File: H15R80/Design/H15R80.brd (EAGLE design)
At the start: 34.6 x 30 mm, 49 parts, among them P1 HEXABIT_17.32_NO_P3_P6, U1 STM32F091CBU6, U2 DAC8760RHA, U3 OPA192, X1 XTALL_CSTCE8M00G52

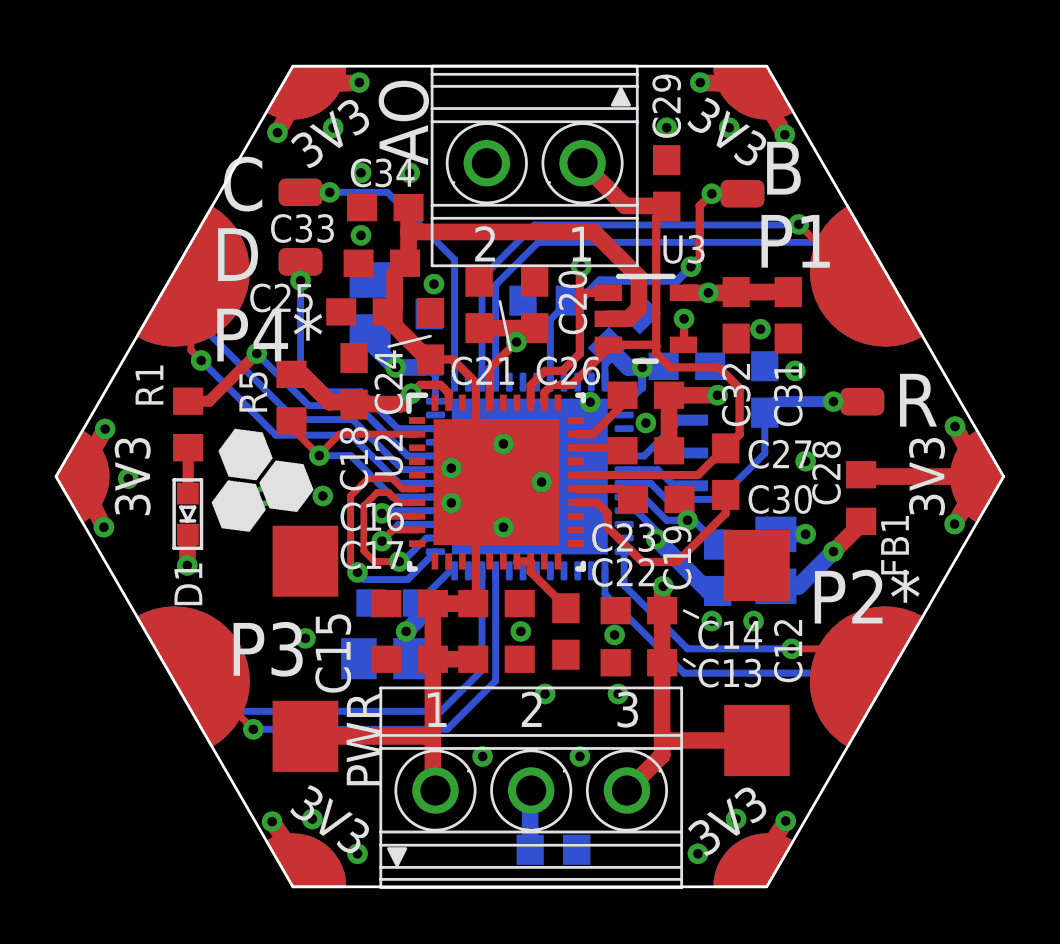
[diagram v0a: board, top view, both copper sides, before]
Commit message: Changing MCU to STM32G0
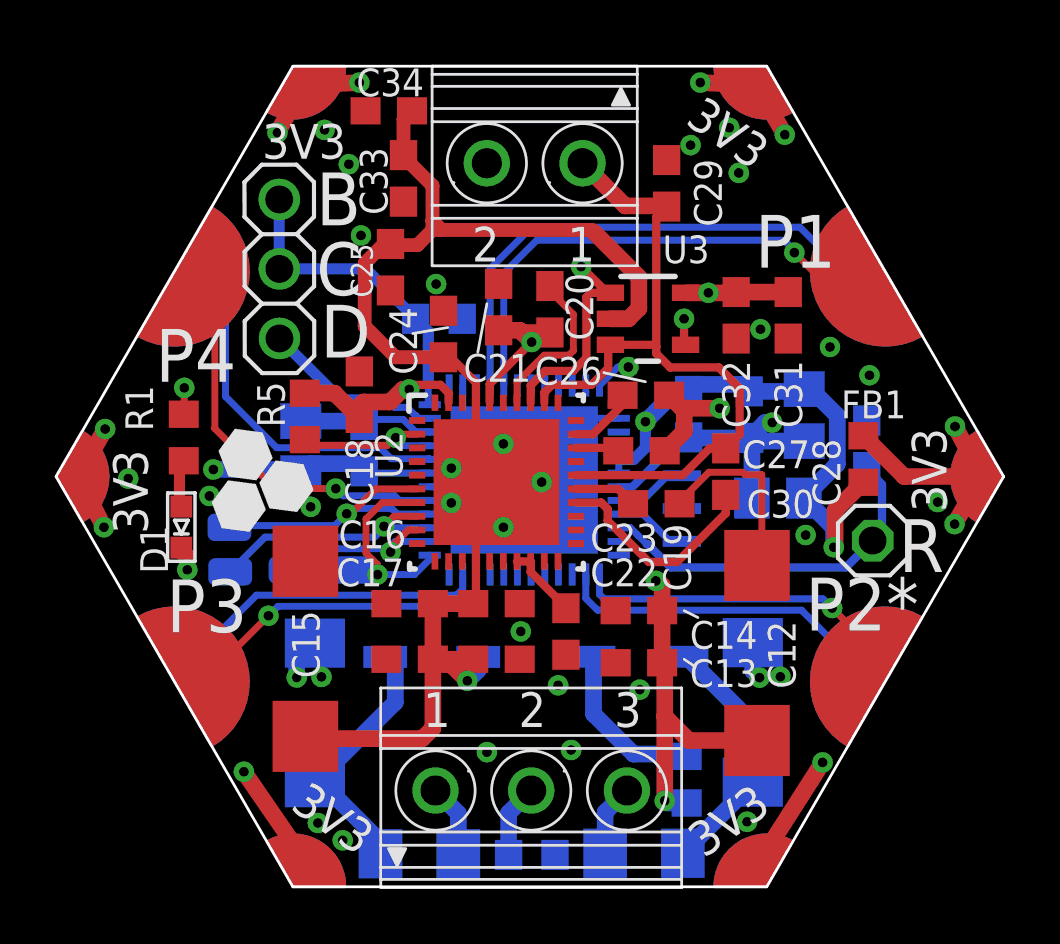
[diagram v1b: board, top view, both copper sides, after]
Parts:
- removed B, C, D, R: PAD1, Hexabitz:PAD1
- removed C6, C9: 100nF, Hexabitz:C-0603
- added CS, MISO, MOSI, SCK: PAD4, HEXABITZ_CONNECTION_PARTS:PAD4
- added D2, D3: DIOD-SOD-123, HEXABITZ_RCLS:SOD123
- added F1, F2: NANOSMDC035F-2120, HEXABITZ_RCLS:R1206
- added JP1: R, HEXABITZ_USER_INTERFACE_PARTS:1X01
- added JP2: (no value), pinhead:1X03
- added R4: 10R, Hexabitz:R-0603
- added TVS1, TVS2: SMBJ30CA, HEXABITZ_RCLS:DO214AA
- C1: value 10nF -> 100nF
- C2: value 1.00uF -> 1uF
- U1: value STM32F091CBU6 -> STM32G0B1CEU6NUFQFPN48_STM32_STM; device Hexabitz:STM32F091CBU6 -> HEXABITZ_ICs:UFQFPN48_STM32_STM
- moved C4 17.7 mm to (44.7, 36.9), turned to 270 degrees
- moved C7 5.75 mm to (26.2, 35.7)
- moved C1 5.71 mm to (40.4, 36.9), turned to 270 degrees
- moved C3 5.51 mm to (42.6, 36.9), turned to 269.6 degrees
- moved C5 4.70 mm to (28.6, 35.7)
- moved C8 4.23 mm to (46.9, 35.8)
- moved R3 3.98 mm to (31.3, 40.4), turned to 0 degrees
- moved C34 3.54 mm to (29.5, 48.0)
- moved C33 3.20 mm to (30.0, 45.5), turned to 270 degrees
- moved C2 2.28 mm to (43.7, 33.8), turned to 0 degrees
- moved X1 2.05 mm to (40.2, 33.4), turned to 180 degrees
- moved C25 1.89 mm to (29.5, 42.3), turned to 270 degrees
- moved FB1 1.43 mm to (46.8, 35.3)
- moved R5 0.84 mm to (26.4, 36.8)
- moved R2 0.81 mm to (34.7, 20.8)
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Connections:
- removed net B1: B.P$1, B.P$2, R3.2, U1.P$44
- removed net R1: C8.1, R.P$1, R.P$2, U1.P$7
- removed net UART1_RX*: P1.PAD_PD5, U1.P$31
- removed net UART1_TX*: P1.PAD_PU5, U1.P$30
- removed net UART2_RX*: P1.PAD_PD2, U1.P$13
- removed net UART2_TX*: P1.PAD_PU2, U1.P$12
- removed net UART4_RX: U1.P$11
- removed net UART4_TX: U1.P$10
- removed net UART6_RX: U1.P$15
- removed net UART6_TX: U1.P$14
- new net CLK: JP2.1, JP2.2, R3.2, U1.36
- new net DATA: JP2.3, U1.35
- new net N$12: F2.1, PWR.1
- new net N$15: D3.2, F2.2, TVS2.A
- new net N$16: D2.1, F1.2, TVS1.C
- new net N$17: D2.2, R4.2
- new net UART1_RX: P1.PAD_PD5, U1.32
- new net UART1_TX: P1.PAD_PU5, U1.29
- new net UART2_RX: P1.PAD_PD2, U1.14
- new net UART2_TX: P1.PAD_PU2, U1.13
- net +15V: now also R4.1; no longer PWR.3
- net -15V: now also D3.1; no longer PWR.1
- net AO_ALARM: now also U1.33; no longer U1.P$29
- net GND: now also U1.1, U1.18, U1.19, U1.2, U1.30, U1.34, U1.37, U1.38, U1.49; no longer C3.2, C4.2, C6.2, C9.2, U1.EP, U1.P$16, U1.P$17, U1.P$18, U1.P$19, U1.P$2, U1.P$20, U1.P$23, U1.P$3, U1.P$35, U1.P$38, U1.P$4, U1.P$41, U1.P$42, U1.P$43, U1.P$47
- net N$3: now also U1.48; no longer U1.P$32
- net N$5: now also C8.1, JP1.1, U1.10; no longer U1.P$5, X1.P$1
- net N$6: now also U1.9, X1.P$1; no longer U1.P$6, X1.P$3
- net N$7: now also U1.8, X1.P$3; no longer D.P$1, D.P$2, U1.P$34
- net N$9: now also F1.1, PWR.3; no longer C.P$1, C.P$2, U1.P$37
- net SPI2_CS: now also CS.P$1, U1.28; no longer U1.P$25
- net SPI2_MISO: now also MISO.P$1, U1.26; no longer U1.P$27
- net SPI2_MOSI: now also MOSI.P$1, U1.27; no longer U1.P$28
- net SPI2_SCK: now also SCK.P$1, U1.25; no longer U1.P$26
- net UART3_RX: now also U1.23; no longer U1.P$22
- net UART3_TX: now also U1.22; no longer U1.P$21
- net UART5_RX: now also U1.40; no longer U1.P$40
- net UART5_TX: now also U1.41; no longer U1.P$39
- net VDD: now also U1.31; no longer C3.1, C4.1, C6.1, C9.1, U1.P$1, U1.P$24, U1.P$36, U1.P$48
- net VDDA: now also C3.1, C4.1, U1.4, U1.5, U1.6; no longer U1.P$9
- net VSSA: now also C3.2, C4.2, TVS1.A, TVS2.C, U1.7; no longer U1.P$8
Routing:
- net VDD: track 127.1 -> 106.6 mm, vias 13 -> 11
- net VSSA: track 9.70 -> 29.3 mm, vias 17 -> 16
- net UART1_RX: track 0.00 -> 15.5 mm
- net GND: track 1.13 -> 16.0 mm, vias 19 -> 18
- net UART1_TX: track 0.00 -> 14.7 mm, vias 0 -> 1
- net UART1_TX*: track 13.5 -> 0.00 mm, vias 1 -> 0
- net B1: track 13.4 -> 0.00 mm, vias 2 -> 0
- net UART1_RX*: track 12.5 -> 0.00 mm
- net R1: track 12.4 -> 0.00 mm, vias 1 -> 0
- net UART2_TX: track 0.00 -> 12.3 mm, vias 0 -> 1
- net UART2_RX: track 0.00 -> 12.3 mm
- net UART2_RX*: track 11.7 -> 0.00 mm
- net CLK: track 0.00 -> 11.6 mm
- net UART2_TX*: track 11.5 -> 0.00 mm, vias 1 -> 0
- net N$5: track 2.91 -> 13.4 mm
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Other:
- board text added: "+"
- board text added: "-"
- board text added: "15V"
- board text added: "P4"
- board text removed: "+15V"
- board text removed: "-15V"
- board text removed: "P4*"

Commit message: Replace the blind vias with through hole ones
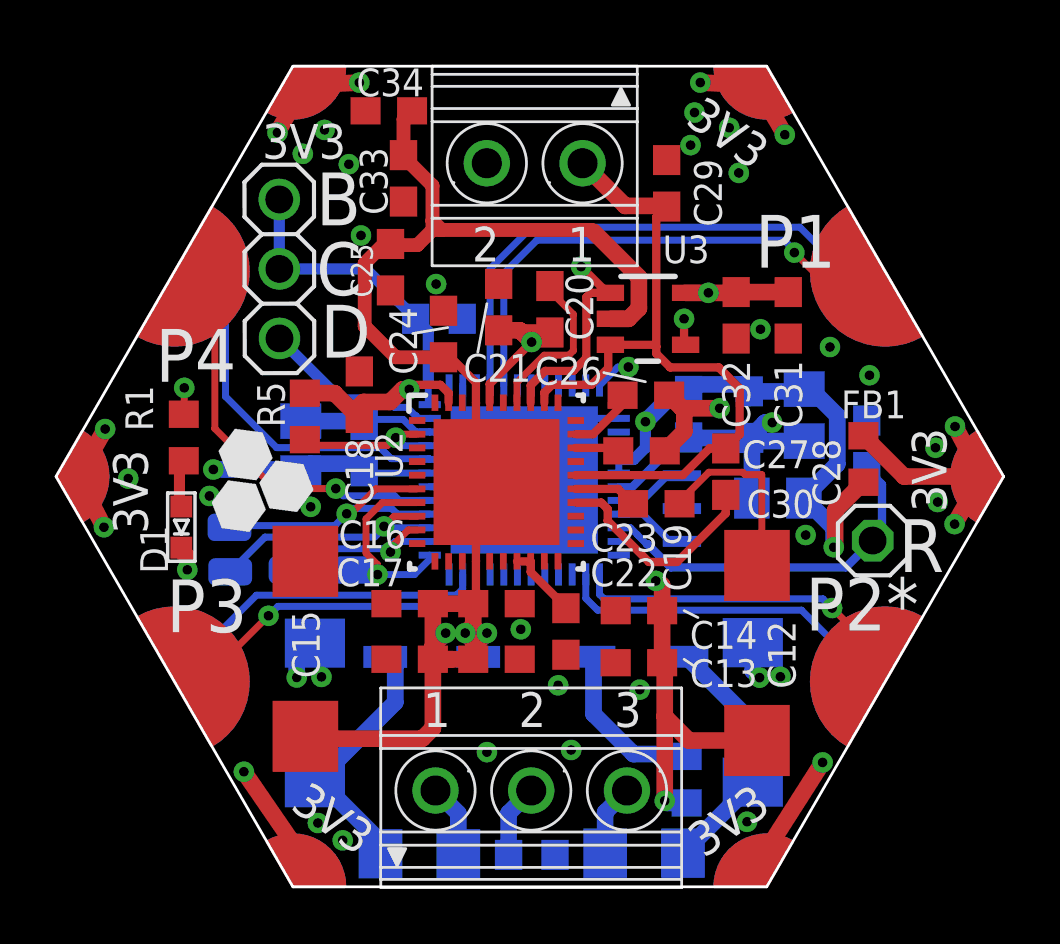
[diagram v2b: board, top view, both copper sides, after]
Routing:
- net -15V: track 51.3 -> 63.2 mm, vias 6 -> 3
- net GND: vias 18 -> 16
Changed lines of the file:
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@@
 <drawing>
 <settings>
-<setting alwaysvectorfont="no"/>
+<setting alwaysvectorfont="yes"/>
 <setting verticaltext="up"/>
 </settings>
@@
 <via x="44.704" y="32.48025" extent="1-16" drill="0.35"/>
 <via x="49.53" y="33.68675" extent="1-16" drill="0.35"/>
-<via x="32.385" y="35.814" extent="15-16" drill="0.35"/>
-<via x="34.798" y="35.814" extent="15-16" drill="0.35"/>
-<via x="35.052" y="32.766" extent="15-16" drill="0.35"/>
-<via x="32.385" y="32.766" extent="15-16" drill="0.35"/>
-<via x="33.655" y="34.29" extent="15-16" drill="0.35"/>
 <contactref element="X1" pad="P$2"/>
 <contactref element="U1" pad="49"/>
@@
 <contactref element="U1" pad="19"/>
 <contactref element="U1" pad="18"/>
+<via x="40.64" y="47.926625" extent="1-16" drill="0.35"/>
+<via x="26.32075" y="46.4185" extent="1-16" drill="0.35"/>
+<via x="49.450625" y="35.671125" extent="1-16" drill="0.35"/>
 </signal>
 <signal name="VDD">
@@
 <via x="43.019346875" y="27.2669" extent="1-16" drill="0.35"/>
 <via x="27.003375" y="27.294203125" extent="1-16" drill="0.35"/>
-<via x="34.29" y="28.956" extent="1-16" drill="0.35"/>
+<via x="34.29" y="29.035375" extent="1-16" drill="0.35"/>
 <via x="31.194375" y="41.656" extent="1-16" drill="0.35"/>
 <via x="43.053" y="40.005" extent="1-16" drill="0.35"/>
@@
 <wire x1="32.651" y1="30.072" x2="32.551" y2="29.972" width="0.3048" layer="1"/>
 <wire x1="31.076" y1="25.420315625" x2="31.076" y2="27.94" width="0.6096" layer="1"/>
-<wire x1="31.076" y1="27.94" x2="31.816040625" y2="27.94" width="0.6096" layer="1"/>
-<wire x1="31.816040625" y1="27.94" x2="32.551" y2="27.94" width="0.6096" layer="1"/>
+<wire x1="31.076" y1="27.94" x2="32.551" y2="27.94" width="0.6096" layer="1"/>
 <wire x1="31.076" y1="27.94" x2="31.076" y2="29.972" width="0.6096" layer="1"/>
 <wire x1="31.076" y1="29.972" x2="32.551" y2="29.972" width="0.6096" layer="1"/>
@@
 <wire x1="30.6928625" y1="25.037178125" x2="26.499821875" y2="25.037178125" width="0.6096" layer="1"/>
 <wire x1="30.6928625" y1="25.037178125" x2="31.076" y2="25.420315625" width="0.6096" layer="1"/>
-<via x="31.75" y="34.925" extent="1-2" drill="0.35"/>
-<via x="31.75" y="33.655" extent="1-2" drill="0.35"/>
-<via x="33.655" y="32.766" extent="1-2" drill="0.35"/>
-<via x="33.655" y="35.814" extent="1-2" drill="0.35"/>
-<via x="35.052" y="34.417" extent="1-2" drill="0.35"/>
 <polygon width="0.254" layer="2">
 <vertex x="31.242" y="36.83"/>
@@
 <wire x1="29.287471875" y1="43.12195" x2="29.525596875" y2="43.12195" width="0.508" layer="1"/>
 <contactref element="D3" pad="1"/>
-<wire x1="32.734353125" y1="28.025728125" x2="32.734353125" y2="27.547671875" width="0.6096" layer="16"/>
-<wire x1="32.734353125" y1="27.547671875" x2="32.336740625" y2="27.150059375" width="0.6096" layer="16"/>
-<via x="32.336740625" y="27.150059375" extent="1-16" drill="0.35"/>
-<wire x1="32.336740625" y1="27.150059375" x2="31.816040625" y2="27.670759375" width="0.6096" layer="1"/>
-<wire x1="31.816040625" y1="27.670759375" x2="31.816040625" y2="27.94" width="0.6096" layer="1"/>
+<wire x1="32.734353125" y1="28.025728125" x2="32.734353125" y2="28.579546875" width="0.6096" layer="16"/>
+<wire x1="32.734353125" y1="28.579546875" x2="33.051115625" y2="28.896309375" width="0.6096" layer="16"/>
+<via x="33.051115625" y="28.896309375" extent="1-16" drill="0.35"/>
+<wire x1="31.076" y1="27.94" x2="31.77730625" y2="27.94" width="0.6096" layer="1"/>
 <wire x1="31.061659375" y1="43.634659375" x2="30.507940625" y2="43.080940625" width="0.508" layer="1"/>
 <wire x1="30.507940625" y1="43.080940625" x2="29.56660625" y2="43.080940625" width="0.508" layer="1"/>
@@
 <wire x1="30.002478125" y1="46.3143625" x2="31.061659375" y2="45.25518125" width="0.508" layer="1"/>
 <wire x1="31.396940625" y1="43.634659375" x2="31.061659375" y2="43.969940625" width="0.508" layer="1"/>
+<via x="32.257365625" y="28.896309375" extent="1-16" drill="0.35"/>
+<via x="31.542990625" y="28.896309375" extent="1-16" drill="0.35"/>
+<wire x1="31.542990625" y1="28.896309375" x2="31.076" y2="28.42931875" width="0.6096" layer="1"/>
+<wire x1="31.076" y1="28.42931875" x2="31.076" y2="27.94" width="0.6096" layer="1"/>
+<wire x1="32.257365625" y1="28.896309375" x2="32.551" y2="28.602675" width="0.6096" layer="1"/>
+<wire x1="32.551" y1="28.602675" x2="32.551" y2="27.94" width="0.6096" layer="1"/>
+<wire x1="32.257365625" y1="28.896309375" x2="32.551" y2="29.18994375" width="0.6096" layer="1"/>
+<wire x1="32.551" y1="29.18994375" x2="32.551" y2="29.972" width="0.6096" layer="1"/>
+<wire x1="31.542990625" y1="28.896309375" x2="32.257365625" y2="28.896309375" width="0.6096" layer="2"/>
+<wire x1="32.257365625" y1="28.896309375" x2="33.051115625" y2="28.896309375" width="0.6096" layer="2"/>
+<wire x1="33.1390625" y1="34.6471875" x2="33.17875" y2="34.6075" width="0.6096" layer="2"/>
+<wire x1="33.17875" y1="34.6075" x2="32.257365625" y2="33.686115625" width="0.6096" layer="2"/>
+<wire x1="32.257365625" y1="33.686115625" x2="32.257365625" y2="28.896309375" width="0.6096" layer="2"/>
+<wire x1="33.051115625" y1="28.896309375" x2="32.551" y2="28.39619375" width="0.6096" layer="1"/>
+<wire x1="32.551" y1="28.39619375" x2="32.551" y2="27.94" width="0.6096" layer="1"/>
 </signal>
 <signal name="AO_ALARM">
